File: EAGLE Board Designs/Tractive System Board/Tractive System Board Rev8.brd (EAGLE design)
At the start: 200 x 65 mm, 138 parts, among them J1 CONNECTOR-5_MICRO_V7S_, J2 CONNECTOR-5_MICRO_V6S_, J3 CONNECTOR-8_μF_T_V_BLACK, K1 RELAY_SPST_NO_D_24, Q2 TRANSISTOR_N_MOS__PMV15ENEA, U10 LTC6994-2, U5 RELAY_SOLIDSTATE_NO_AB38S-Q-A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, U6 LT8315, U7 AMC3330_AIRGAP, U8 AMC3330_AIRGAP

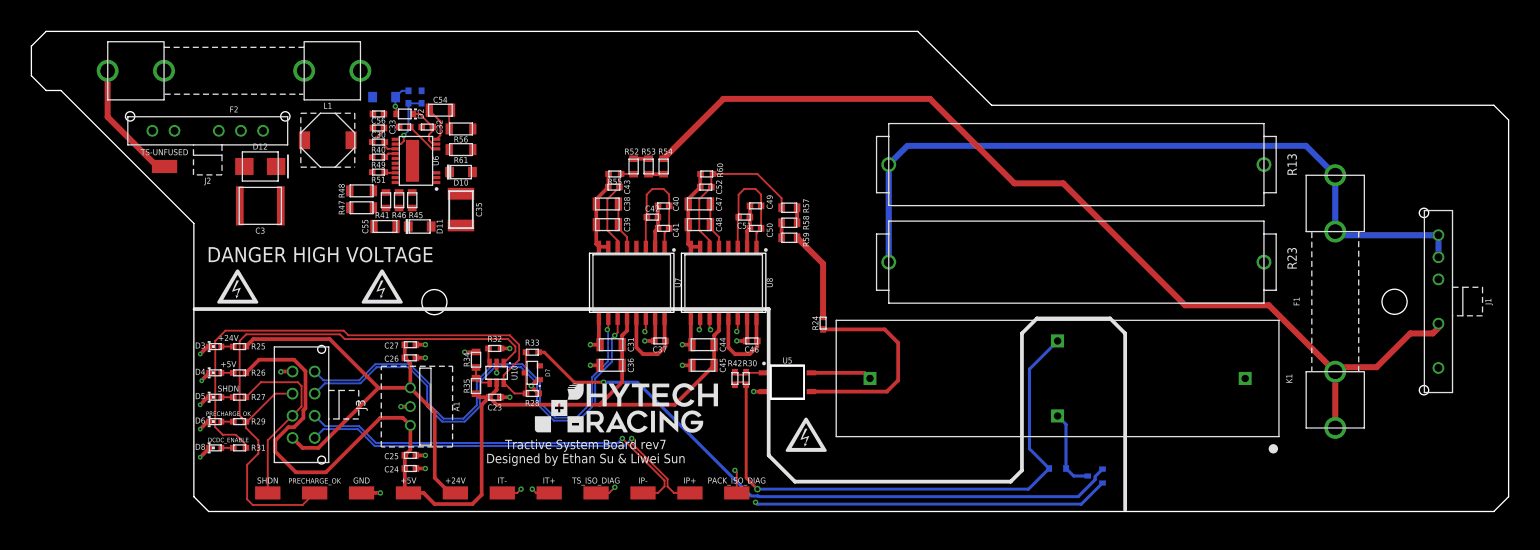
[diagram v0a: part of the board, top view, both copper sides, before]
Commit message: tsb-rev8-layout-update
replaced m3 mounting holes for m4s
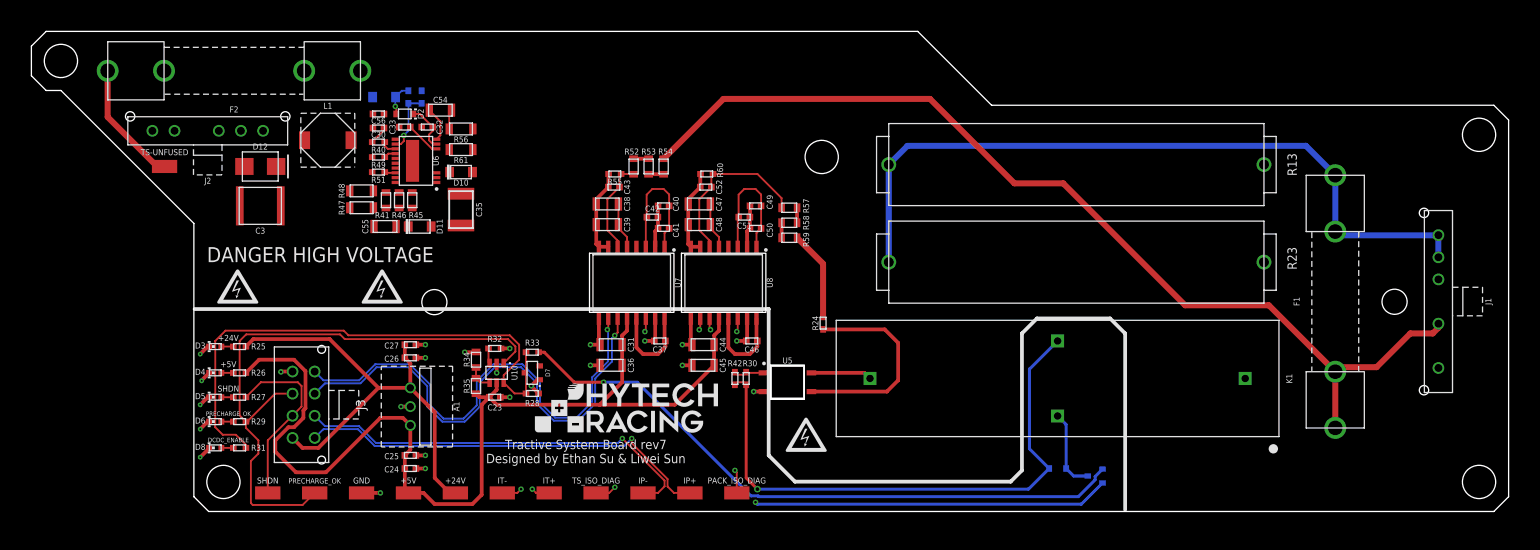
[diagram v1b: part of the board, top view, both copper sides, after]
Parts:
- added U$1, U$2, U$4, U$5, U$6: (no value), HyTechManufacturing:MOUNTING_M4
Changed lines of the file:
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@@
 <setting verticaltext="up"/>
 </settings>
-<grid distance="10" unitdist="mil" unit="mil" style="lines" multiple="1" display="no" altdistance="5" altunitdist="mil" altunit="mil"/>
+<grid distance="10" unitdist="mil" unit="mm" style="lines" multiple="1" display="no" altdistance="5" altunitdist="mil" altunit="mil"/>
 <layers>
 <layer number="1" name="Top" color="4" fill="1" visible="yes" active="yes"/>
@@
 <layer number="25" name="tNames" color="7" fill="1" visible="yes" active="yes"/>
 <layer number="26" name="bNames" color="7" fill="1" visible="yes" active="yes"/>
-<layer number="27" name="tValues" color="7" fill="1" visible="no" active="yes"/>
+<layer number="27" name="tValues" color="7" fill="1" visible="yes" active="yes"/>
 <layer number="28" name="bValues" color="7" fill="1" visible="no" active="yes"/>
-<layer number="29" name="tStop" color="7" fill="3" visible="no" active="yes"/>
+<layer number="29" name="tStop" color="7" fill="3" visible="yes" active="yes"/>
 <layer number="30" name="bStop" color="7" fill="6" visible="no" active="yes"/>
 <layer number="31" name="tCream" color="7" fill="4" visible="no" active="yes"/>
@@
 <layer number="105" name="tPlate" color="7" fill="1" visible="no" active="yes"/>
 <layer number="106" name="bPlate" color="7" fill="1" visible="no" active="yes"/>
-<layer number="107" name="Crop" color="7" fill="1" visible="no" active="yes"/>
+<layer number="107" name="Crop" color="7" fill="1" visible="yes" active="yes"/>
 <layer number="108" name="tplace-old" color="10" fill="1" visible="no" active="yes"/>
 <layer number="109" name="ref-old" color="11" fill="1" visible="no" active="yes"/>
@@
 <attribute name="VOLTAGE_MAX" value="" x="-51.054" y="-44.704" size="1.778" layer="27" display="off"/>
 </element>
+<element name="U$1" library="HyTechManufacturing" package="MOUNTING_M4" value="" x="4" y="-4" smashed="yes"/>
+<element name="U$2" library="HyTechManufacturing" package="MOUNTING_M4" value="" x="26" y="-61" smashed="yes"/>
+<element name="U$4" library="HyTechManufacturing" package="MOUNTING_M4" value="" x="196" y="-14" smashed="yes"/>
+<element name="U$5" library="HyTechManufacturing" package="MOUNTING_M4" value="" x="196" y="-61" smashed="yes"/>
+<element name="U$6" library="HyTechManufacturing" package="MOUNTING_M4" value="" x="107" y="-17" smashed="yes"/>
 </elements>
 <signals>
@@
 <wire x1="38.354" y1="-62.484" x2="36.722" y2="-64.116" width="0.254" layer="1"/>
 <wire x1="36.722" y1="-64.116" x2="29.972" y2="-64.116" width="0.254" layer="1"/>
-<wire x1="29.972" y1="-64.116" x2="29.21" y2="-63.354" width="0.254" layer="1"/>
+<wire x1="29.972" y1="-64.116" x2="29.718" y2="-63.862" width="0.254" layer="1"/>
 <wire x1="63.942" y1="-44.918" x2="65.532" y2="-43.328" width="0.254" layer="1"/>
 <wire x1="65.532" y1="-43.328" x2="65.532" y2="-42.672" width="0.254" layer="1"/>
@@
 <wire x1="28.194" y1="-51.982" x2="29.044" y2="-52.832" width="0.254" layer="1"/>
 <wire x1="64.516" y1="-41.656" x2="42.418" y2="-41.656" width="0.254" layer="1"/>
-<wire x1="29.21" y1="-58.674" x2="30.734" y2="-57.15" width="0.254" layer="1"/>
+<wire x1="29.718" y1="-58.166" x2="30.734" y2="-57.15" width="0.254" layer="1"/>
 <wire x1="30.734" y1="-57.15" x2="30.734" y2="-55.372" width="0.254" layer="1"/>
 <wire x1="29.044" y1="-53.682" x2="29.044" y2="-52.832" width="0.254" layer="1"/>
-<wire x1="29.21" y1="-63.354" x2="29.21" y2="-58.674" width="0.254" layer="1"/>
+<wire x1="29.718" y1="-63.862" x2="29.718" y2="-58.166" width="0.254" layer="1"/>
 <wire x1="30.734" y1="-55.372" x2="29.044" y2="-53.682" width="0.254" layer="1"/>
 </signal>

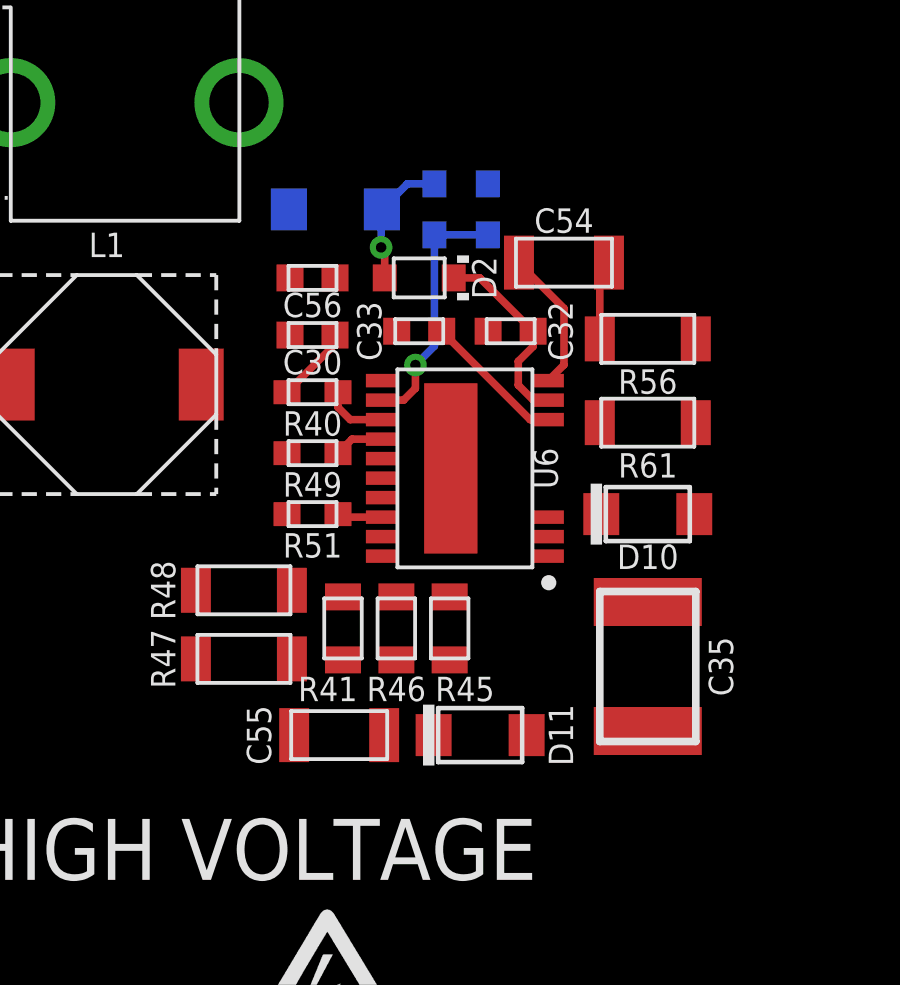
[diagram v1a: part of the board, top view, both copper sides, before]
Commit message: tsb-rev8-layout-update
more buck routing
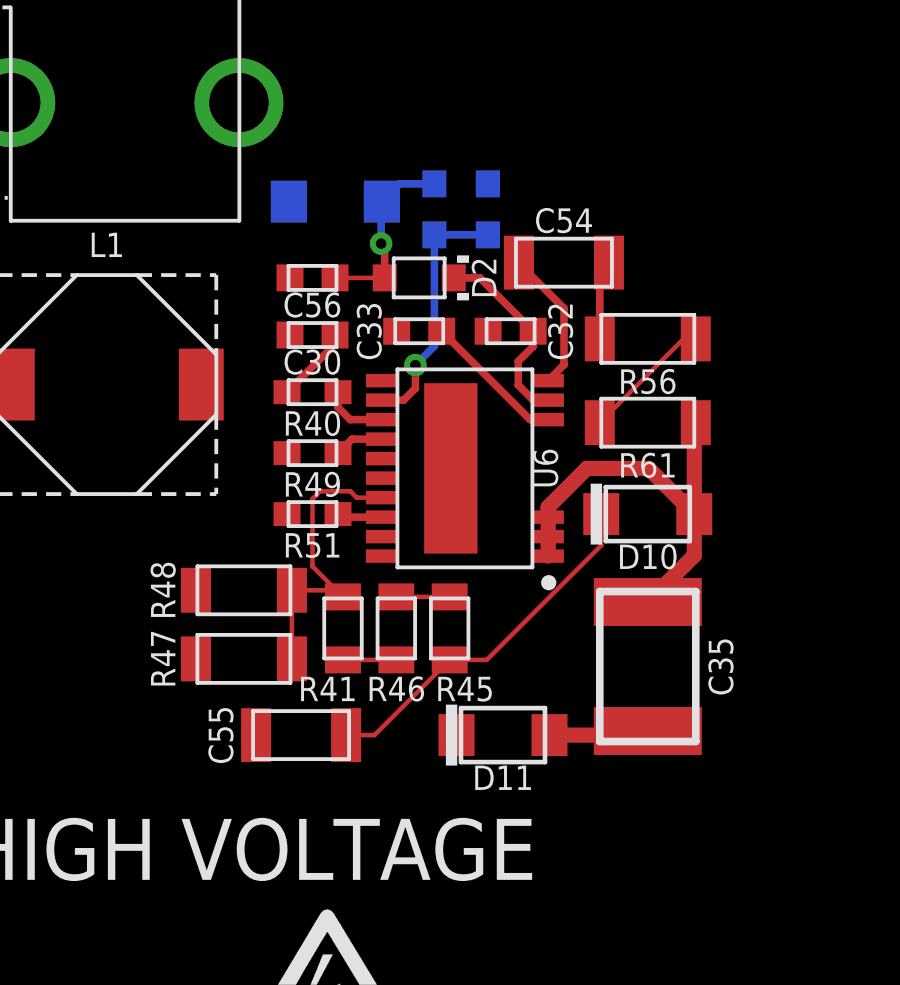
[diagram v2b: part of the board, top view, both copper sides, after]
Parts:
- moved C55 1.27 mm to (46.6, -26.4), turned to 180 degrees
- moved D11 0.76 mm to (53.3, -26.4)
- moved D9 0.25 mm to (47.8, -8.64)
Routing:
- net TS+FUSED: track 134.2 -> 148.5 mm
- net N$46: track 0.00 -> 12.2 mm
- net EN/UVLO: track 0.00 -> 10.3 mm
- net N$34: track 0.25 -> 4.61 mm
- net TS-FUSED: track 58.9 -> 62.2 mm
- net N$55: track 4.45 -> 6.26 mm
- net N$4: track 0.00 -> 1.78 mm
- net N$1: track 0.00 -> 1.78 mm

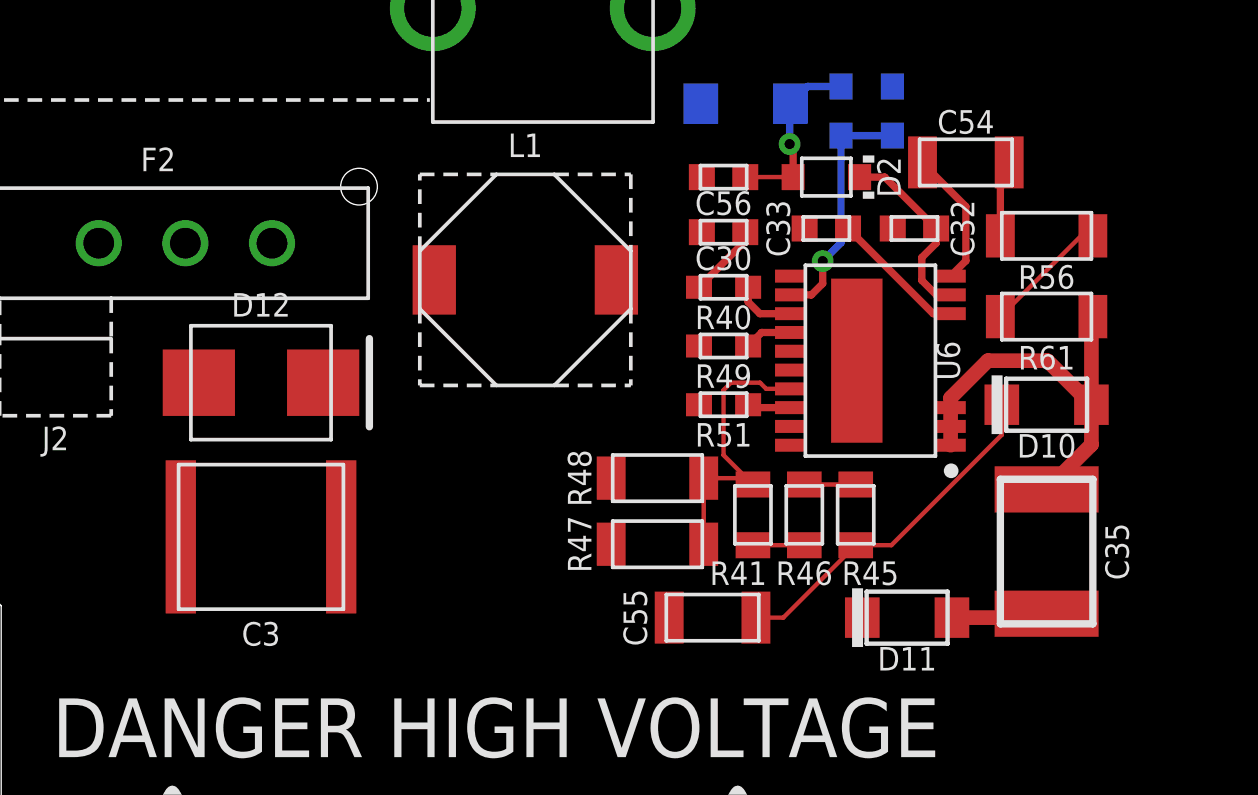
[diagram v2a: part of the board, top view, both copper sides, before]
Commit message: tsb-rev8-layout-update
added PGND plane
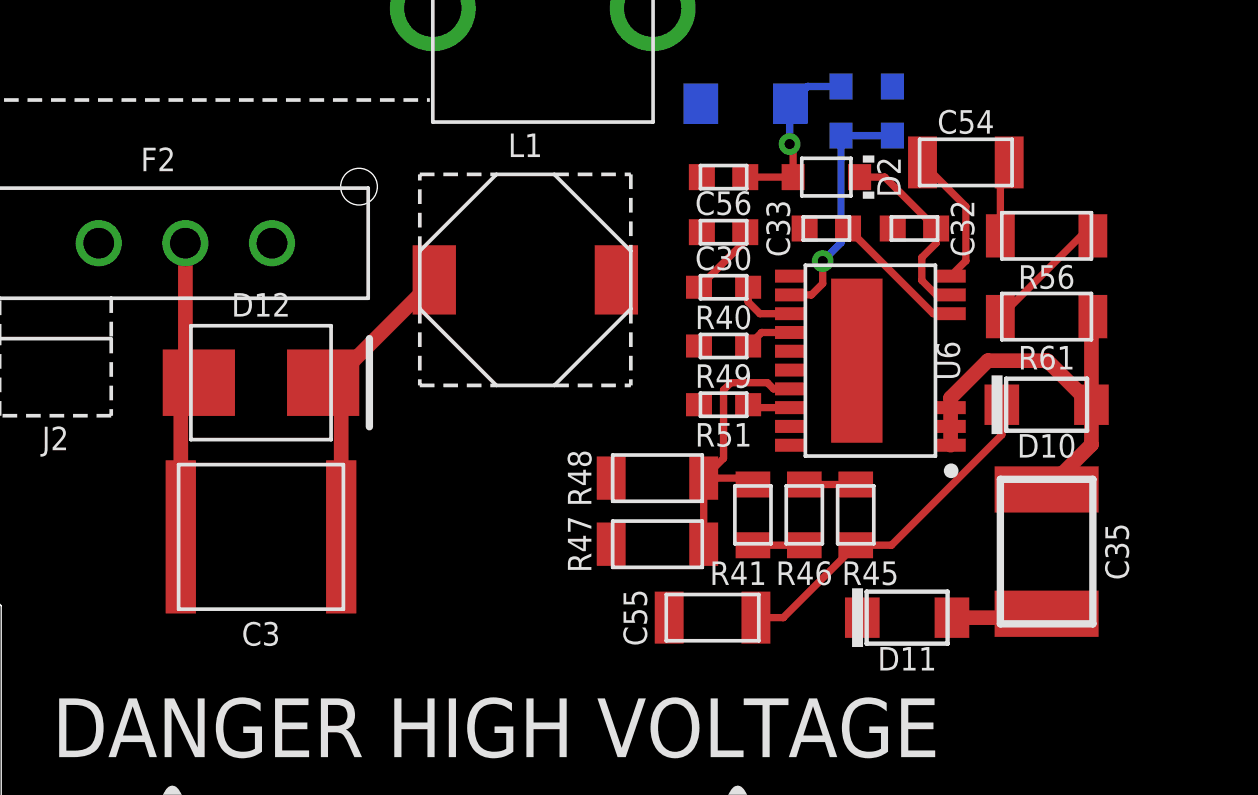
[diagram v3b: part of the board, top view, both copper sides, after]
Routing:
- net TS+12V: track 0.00 -> 10.9 mm
- net TS-FUSED: track 62.2 -> 72.8 mm
- added copper zone on layer 2, net PGND

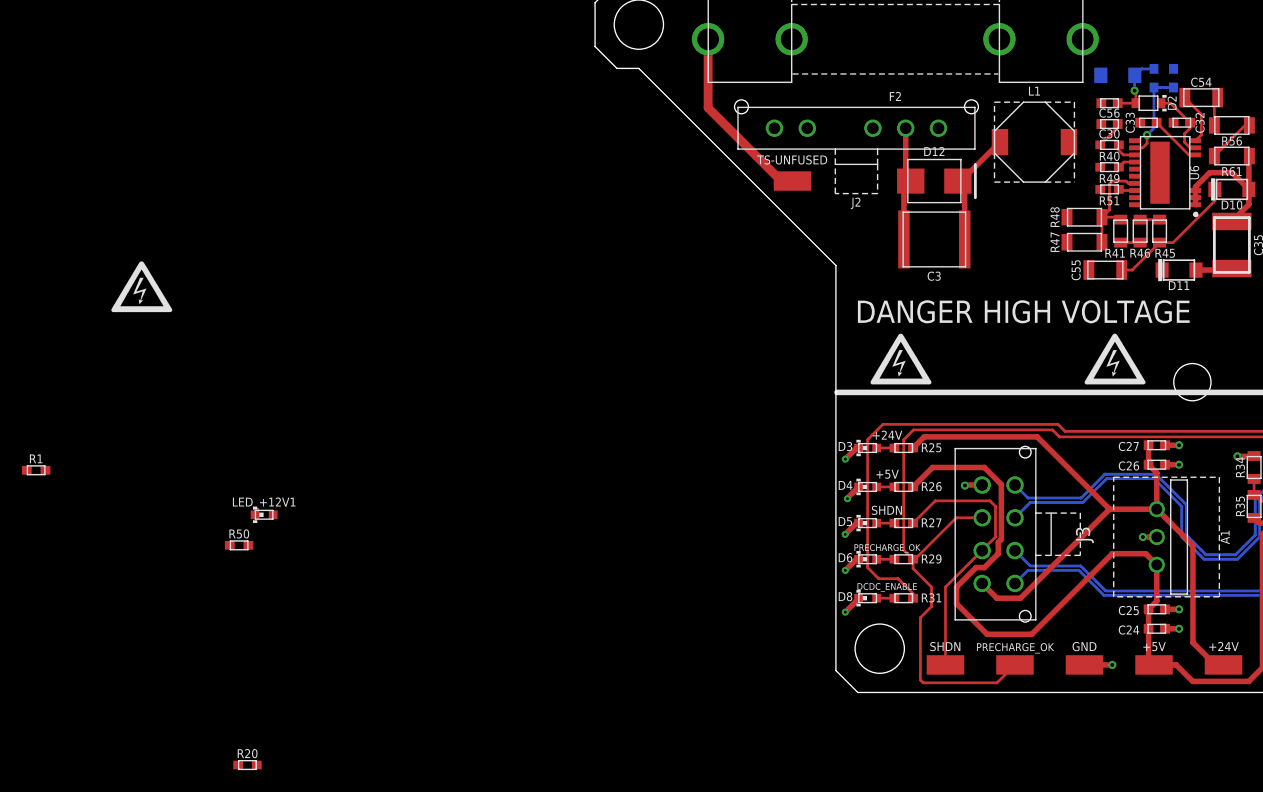
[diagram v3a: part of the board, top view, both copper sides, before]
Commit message: tsb-rev8-layout-update
redid PGND plane and routed AIL
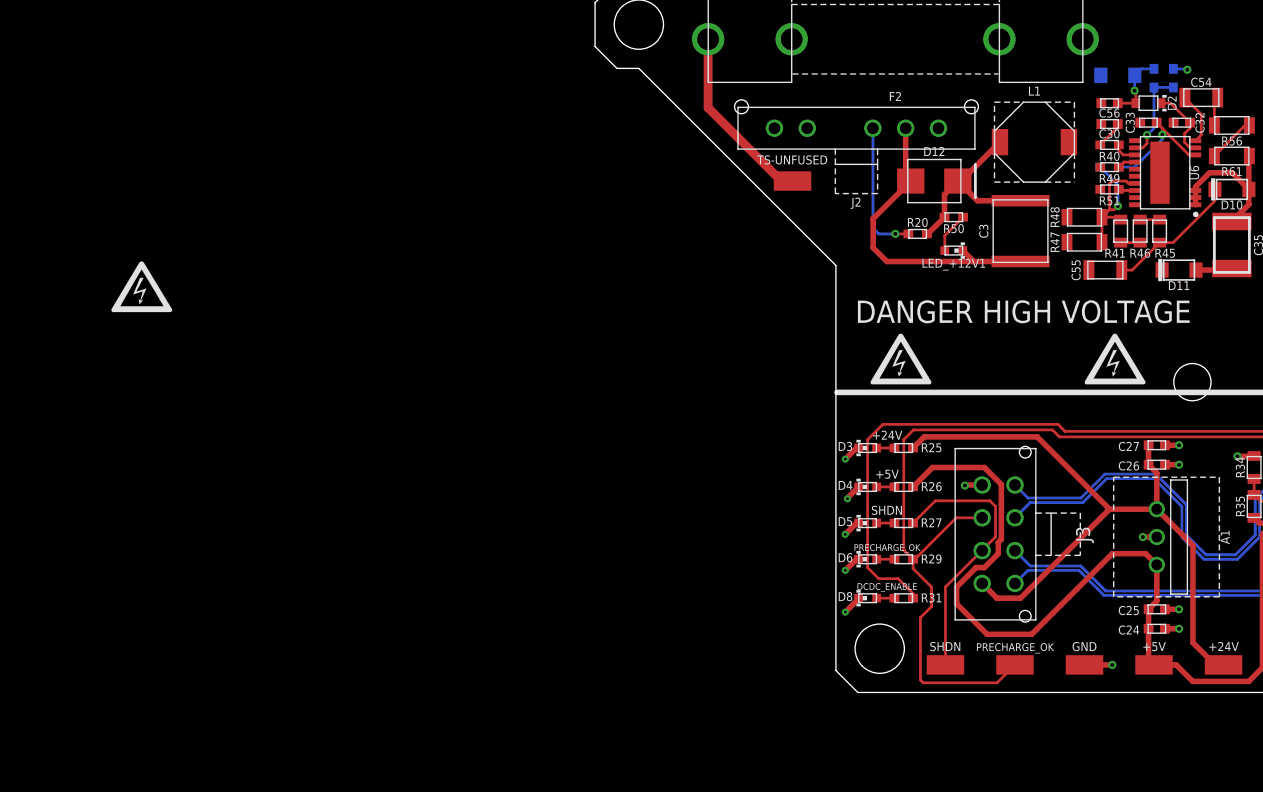
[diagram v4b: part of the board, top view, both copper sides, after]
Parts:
- moved R1 101.9 mm to (47.0, -17.0), flipped to the bottom
- moved R20 78.1 mm to (29.5, -23.1)
- moved R50 71.8 mm to (32.8, -21.6), turned to 180 degrees
- moved LED_+12V1 67.5 mm to (32.8, -24.6), turned to 180 degrees
- moved C3 7.91 mm to (38.9, -22.9), turned to 270 degrees
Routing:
- net TS-FUSED: track 72.8 -> 91.0 mm
- net AIL+: track 0.00 -> 12.6 mm, vias 0 -> 1
- net TS+12V: track 10.9 -> 18.7 mm
- net INTVCC: track 4.77 -> 10.8 mm, vias 0 -> 1
- net EN/UVLO: track 9.91 -> 15.0 mm, vias 0 -> 1
- net N$44: track 0.00 -> 3.74 mm
- net PGND: track 0.00 -> 1.31 mm, vias 0 -> 1
